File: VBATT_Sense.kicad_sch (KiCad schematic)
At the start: 3 parts, among them U8 INA229AQDGSRQ1

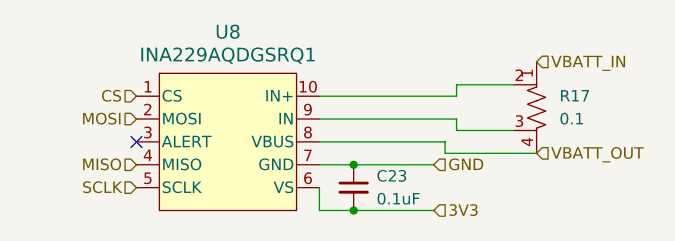
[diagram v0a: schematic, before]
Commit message: Connected topsheet
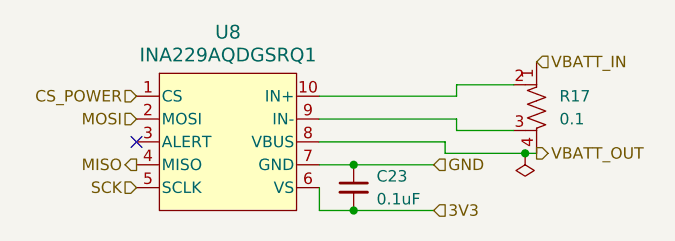
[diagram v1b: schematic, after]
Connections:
- net CS renamed CS_POWER
- net SCLK renamed SCK
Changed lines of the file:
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@@
+		(color 0 0 0 0)
+	)
+	(junction
+		(at 132.08 66.04)
+		(diameter 0)
 		(color 0 0 0 0)
 	)
@@
 	(wire
 		(pts
-			(xy 123.19 66.04) (xy 133.35 66.04)
+			(xy 132.08 66.04) (xy 133.35 66.04)
+		)
+		(stroke
+			(width 0)
+			(type default)
+		)
+	)
+	(wire
+		(pts
+			(xy 123.19 66.04) (xy 132.08 66.04)
 		)
 		(stroke
@@
 		)
 	)
-	(hierarchical_label "CS"
+	(hierarchical_label "CS_POWER"
 		(shape input)
 		(at 88.9 59.69 180)
@@
 	)
 	(hierarchical_label "MISO"
-		(shape input)
+		(shape output)
 		(at 88.9 67.31 180)
 		(effects
@@
 		)
 	)
-	(hierarchical_label "SCLK"
+	(hierarchical_label "SCK"
 		(shape input)
 		(at 88.9 69.85 180)
@@
 	)
 	(hierarchical_label "VBATT_OUT"
-		(shape input)
+		(shape output)
 		(at 133.35 66.04 0)
 		(effects
@@
 		)
 	)
+	(symbol
+		(lib_id "power:PWR_FLAG")
+		(at 132.08 66.04 180)
+		(unit 1)
+		(exclude_from_sim no)
+		(in_bom yes)
+		(on_board yes)
+		(dnp no)
+		(fields_autoplaced yes)
+		(property "Reference" "#FLG02"
+			(at 132.08 67.945 0)
+			(effects
+				(font
+					(size 1.27 1.27)
+				)
+				(hide yes)
+			)
+		)
+		(property "Value" "PWR_FLAG"
+			(at 132.08 71.12 0)
+			(effects
+				(font
+					(size 1.27 1.27)
+				)
+				(hide yes)
+			)
+		)
+		(property "Footprint" ""
+			(at 132.08 66.04 0)
+			(effects
+				(font
+					(size 1.27 1.27)
+				)
+				(hide yes)
+			)
+		)
+		(property "Datasheet" "~"
+			(at 132.08 66.04 0)
+			(effects
+				(font
+					(size 1.27 1.27)
+				)
+				(hide yes)
+			)
+		)
+		(property "Description" "Special symbol for telling ERC where power comes from"
+			(at 132.08 66.04 0)
+			(effects
+				(font
+					(size 1.27 1.27)
+				)
+				(hide yes)
+			)
+		)
+		(pin "1"
+		)
+		(instances
+			(project ""
+				(path "/2c2eadf0-5503-4531-8753-1a232087fe8c/ff86f43e-2806-4661-a460-b8d13650ca02/3f1a3f1c-849d-463b-bb98-bc3e98494186"
+					(reference "#FLG02")
+					(unit 1)
+				)
+			)
+		)
+	)

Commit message: Reannotated
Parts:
- renumbered R17 to R15
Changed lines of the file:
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@@
 		(dnp no)
 		(fields_autoplaced yes)
-		(property "Reference" "#FLG02"
+		(property "Reference" "#FLG03"
 			(at 132.08 67.945 0)
 			(effects
@@
 			(project ""
 				(path "/2c2eadf0-5503-4531-8753-1a232087fe8c/ff86f43e-2806-4661-a460-b8d13650ca02/3f1a3f1c-849d-463b-bb98-bc3e98494186"
-					(reference "#FLG02")
+					(reference "#FLG03")
 					(unit 1)
 				)
@@
 		(dnp no)
 		(fields_autoplaced yes)
-		(property "Reference" "R17"
+		(property "Reference" "R15"
 			(at 135.89 59.6899 0)
 			(effects
@@
 			(project "Blaze-NT"
 				(path "/2c2eadf0-5503-4531-8753-1a232087fe8c/ff86f43e-2806-4661-a460-b8d13650ca02/3f1a3f1c-849d-463b-bb98-bc3e98494186"
-					(reference "R17")
-					(unit 1)
-				)
+					(reference "R15")
+					(unit 1)
+				)

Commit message: Footprint selection
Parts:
- C23: footprint (none) -> Capacitor_SMD:C_0603_1608Metric
- R15: footprint (none) -> Resistor_SMD:R_Shunt_Ohmite_LVK24
- U8: footprint VSSOP10_DGS_TEX -> Package_SO:VSSOP-10_3x3mm_P0.5mm
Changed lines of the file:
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@@
 			)
 		)
-		(property "Footprint" "VSSOP10_DGS_TEX"
+		(property "Footprint" "Package_SO:VSSOP-10_3x3mm_P0.5mm"
 			(at 119.126 49.022 0)
 			(effects
@@
 			)
 		)
-		(property "Footprint" ""
+		(property "Footprint" "Capacitor_SMD:C_0603_1608Metric"
 			(at 113.03 69.85 0)
 			(effects
@@
 			)
 		)
-		(property "Footprint" ""
+		(property "Footprint" "Resistor_SMD:R_Shunt_Ohmite_LVK24"
 			(at 135.128 60.96 90)
 			(effects

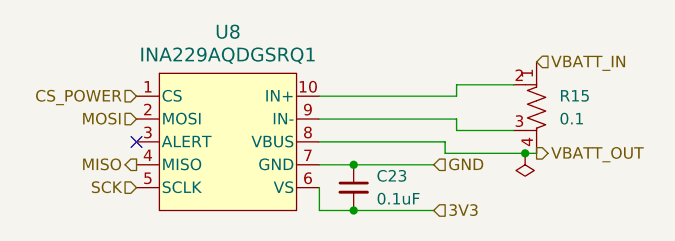
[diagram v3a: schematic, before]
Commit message: Radio footprint selection
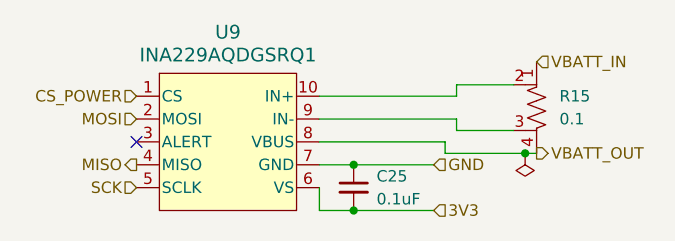
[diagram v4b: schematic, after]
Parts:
- renumbered C23 to C25, U8 to U9
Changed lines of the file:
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@@
 		(on_board yes)
 		(dnp no)
-		(property "Reference" "U8"
+		(property "Reference" "U9"
 			(at 99.06 52.578 0)
 			(effects
@@
 			(project "Blaze-NT"
 				(path "/2c2eadf0-5503-4531-8753-1a232087fe8c/ff86f43e-2806-4661-a460-b8d13650ca02/3f1a3f1c-849d-463b-bb98-bc3e98494186"
-					(reference "U8")
+					(reference "U9")
 					(unit 1)
 				)
@@
 		(dnp no)
 		(fields_autoplaced yes)
-		(property "Reference" "C23"
+		(property "Reference" "C25"
 			(at 115.57 68.5862 0)
 			(effects
@@
 			(project "Blaze-NT"
 				(path "/2c2eadf0-5503-4531-8753-1a232087fe8c/ff86f43e-2806-4661-a460-b8d13650ca02/3f1a3f1c-849d-463b-bb98-bc3e98494186"
-					(reference "C23")
+					(reference "C25")
 					(unit 1)
 				)

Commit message: PCB work
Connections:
- net VBATT_IN: now also R15.4; no longer R15.1
- net VBATT_OUT: now also R15.1; no longer R15.4
- net at U9.10 (IN+): now also R15.3; no longer R15.2
- net at U9.9 (IN-): now also R15.2; no longer R15.3
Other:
- moved on the sheet: R15
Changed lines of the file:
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@@
 	(symbol
 		(lib_id "Device:R_Shunt_US")
-		(at 133.35 60.96 0)
-		(mirror y)
+		(at 133.35 60.96 180)
 		(unit 1)
 		(exclude_from_sim no)
@@
 		(on_board yes)
 		(dnp no)
-		(fields_autoplaced yes)
 		(property "Reference" "R15"
-			(at 135.89 59.6899 0)
+			(at 135.89 62.2301 0)
 			(effects
 				(font
@@
 		)
 		(property "Value" "0.1"
-			(at 135.89 62.2299 0)
+			(at 135.89 59.6901 0)
 			(effects
 				(font

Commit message: Addeed part numbers
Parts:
- C25: LCSC (none) -> C14663
- R15: LCSC (none) -> C6981159
- U9: LCSC (none) -> C2870151
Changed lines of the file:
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@@
+			)
+		)
+		(property "LCSC" "C2870151"
+			(at 99.06 64.77 0)
+			(effects
+				(font
+					(size 1.27 1.27)
+				)
+				(hide yes)
 			)
 		)
@@
 			)
 		)
+		(property "LCSC" "C14663"
+			(at 113.03 69.85 0)
+			(effects
+				(font
+					(size 1.27 1.27)
+				)
+				(hide yes)
+			)
+		)
 		(pin "1"
 		)
@@
 			(at 133.35 60.96 0)
 			(effects
+				(font
+					(size 1.27 1.27)
+				)
+				(hide yes)
+			)
+		)
+		(property "LCSC" "C6981159"
+			(at 133.35 60.96 0)
+			(effects

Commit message: Added Digikey Components
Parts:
- R15: Digikey (none) -> LVK24R100CER
- U9: Digikey (none) -> INA229AQDGSRQ1
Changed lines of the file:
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@@
+			)
+		)
+		(property "Digikey" "INA229AQDGSRQ1"
+			(at 99.06 64.77 0)
+			(effects
+				(font
+					(size 1.27 1.27)
+				)
+				(hide yes)
 			)
 		)
@@
 			)
 		)
+		(property "Digikey" ""
+			(at 113.03 69.85 0)
+			(effects
+				(font
+					(size 1.27 1.27)
+				)
+				(hide yes)
+			)
+		)
 		(pin "1"
 		)
@@
 			(at 133.35 60.96 0)
 			(effects
+				(font
+					(size 1.27 1.27)
+				)
+				(hide yes)
+			)
+		)
+		(property "Digikey" "LVK24R100CER"
+			(at 133.35 60.96 0)
+			(effects
